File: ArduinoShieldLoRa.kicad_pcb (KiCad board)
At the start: 2 copper layers, 68.6 x 53.3 mm, 17 parts, among them J1 CONN_01X03, P1 Power, P2 Analog, P3 Digital, P4 Digital, P5 CONN_01X01, P6 CONN_01X01, P7 CONN_01X01, P8 CONN_01X01, U1 RFM95, U2 74HC4050D, U3 AP2112K-3.3

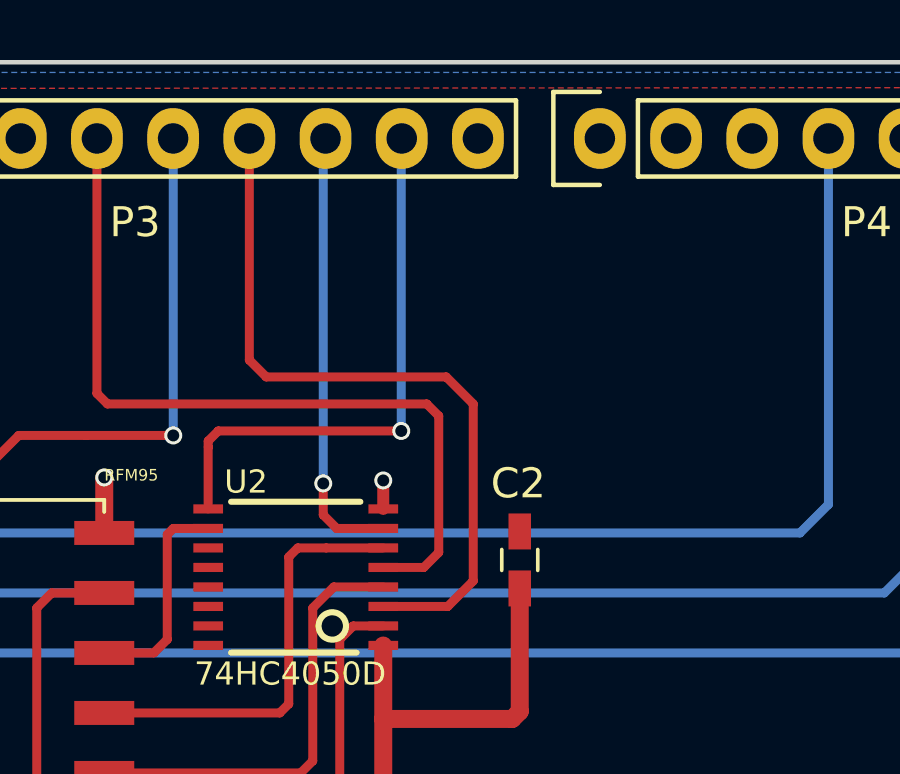
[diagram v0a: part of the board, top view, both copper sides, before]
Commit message: Add resistors
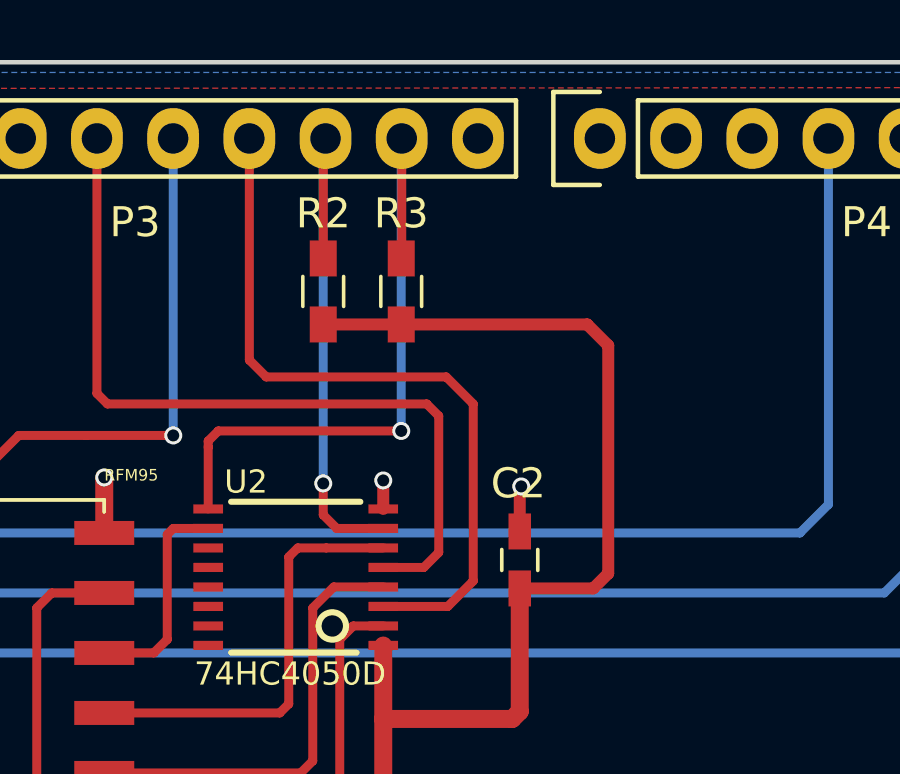
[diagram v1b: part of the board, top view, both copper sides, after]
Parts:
- added R2: 100k, Resistors_SMD:R_0603_HandSoldering, F.Cu at (147.5, 80.7)
- added R3: 100k, Resistors_SMD:R_0603_HandSoldering, F.Cu at (150.1, 80.7)
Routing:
- net +3V3: track 66.5 -> 87.1 mm
- net /10(**/SS): track 14.8 -> 18.8 mm
- net /9(**): track 18.6 -> 22.6 mm
- net GND: track 30.8 -> 32.3 mm, vias 5 -> 6
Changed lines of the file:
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@@
 (kicad_pcb (version 4) (host pcbnew 4.0.6)
   (general
-    (links 38)
-    (no_connects 11)
+    (links 42)
+    (no_connects 14)
     (area 110.922999 72.949999 179.653001 126.440001)
     (thickness 1.6)
     (drawings 27)
-    (tracks 137)
+    (tracks 150)
     (zones 0)
-    (modules 17)
+    (modules 19)
     (nets 52)
   )
@@
       (net 30 +3V3))
   )
+  (module Resistors_SMD:R_0603_HandSoldering (layer F.Cu)
+    (at 147.498 80.665 90)
+    (descr "Resistor SMD 0603, hand soldering")
+    (tags "resistor 0603")
+    (attr smd)
+    (fp_text reference R2 (at 2.6 0 180) (layer F.SilkS)
+      (effects (font (size 1 1) (thickness 0.15)))
+    )
+    (fp_text value 100k (at 0 1.55 90) (layer F.Fab)
+      (effects (font (size 1 1) (thickness 0.15)))
+    )
+    (fp_text user %R (at 0 0 90) (layer F.Fab)
+      (effects (font (size 0.5 0.5) (thickness 0.075)))
+    )
+    (fp_line (start -0.8 0.4) (end -0.8 -0.4) (layer F.Fab) (width 0.1))
+    (fp_line (start 0.8 0.4) (end -0.8 0.4) (layer F.Fab) (width 0.1))
+    (fp_line (start 0.8 -0.4) (end 0.8 0.4) (layer F.Fab) (width 0.1))
+    (fp_line (start -0.8 -0.4) (end 0.8 -0.4) (layer F.Fab) (width 0.1))
+    (fp_line (start 0.5 0.68) (end -0.5 0.68) (layer F.SilkS) (width 0.12))
+    (fp_line (start -0.5 -0.68) (end 0.5 -0.68) (layer F.SilkS) (width 0.12))
+    (fp_line (start -1.96 -0.7) (end 1.95 -0.7) (layer F.CrtYd) (width 0.05))
+    (fp_line (start -1.96 -0.7) (end -1.96 0.7) (layer F.CrtYd) (width 0.05))
+    (fp_line (start 1.95 0.7) (end 1.95 -0.7) (layer F.CrtYd) (width 0.05))
+    (fp_line (start 1.95 0.7) (end -1.96 0.7) (layer F.CrtYd) (width 0.05))
+    (pad 1 smd rect (at -1.1 0 90) (size 1.2 0.9) (layers F.Cu F.Paste F.Mask)
+      (net 30 +3V3))
+    (pad 2 smd rect (at 1.1 0 90) (size 1.2 0.9) (layers F.Cu F.Paste F.Mask)
+      (net 28 "/10(**/SS)"))
+    (model ${KISYS3DMOD}/Resistors_SMD.3dshapes/R_0603.wrl
+      (at (xyz 0 0 0))
+      (scale (xyz 1 1 1))
+      (rotate (xyz 0 0 0))
+    )
+  )
+  (module Resistors_SMD:R_0603_HandSoldering (layer F.Cu)
+    (at 150.098 80.665 90)
+    (descr "Resistor SMD 0603, hand soldering")
+    (tags "resistor 0603")
+    (attr smd)
+    (fp_text reference R3 (at 2.6 0 180) (layer F.SilkS)
+      (effects (font (size 1 1) (thickness 0.15)))
+    )
+    (fp_text value 100k (at 0 1.55 90) (layer F.Fab)
+      (effects (font (size 1 1) (thickness 0.15)))
+    )
+    (fp_text user %R (at 0 0 90) (layer F.Fab)
+      (effects (font (size 0.5 0.5) (thickness 0.075)))
+    )
+    (fp_line (start -0.8 0.4) (end -0.8 -0.4) (layer F.Fab) (width 0.1))
+    (fp_line (start 0.8 0.4) (end -0.8 0.4) (layer F.Fab) (width 0.1))
+    (fp_line (start 0.8 -0.4) (end 0.8 0.4) (layer F.Fab) (width 0.1))
+    (fp_line (start -0.8 -0.4) (end 0.8 -0.4) (layer F.Fab) (width 0.1))
+    (fp_line (start 0.5 0.68) (end -0.5 0.68) (layer F.SilkS) (width 0.12))
+    (fp_line (start -0.5 -0.68) (end 0.5 -0.68) (layer F.SilkS) (width 0.12))
+    (fp_line (start -1.96 -0.7) (end 1.95 -0.7) (layer F.CrtYd) (width 0.05))
+    (fp_line (start -1.96 -0.7) (end -1.96 0.7) (layer F.CrtYd) (width 0.05))
+    (fp_line (start 1.95 0.7) (end 1.95 -0.7) (layer F.CrtYd) (width 0.05))
+    (fp_line (start 1.95 0.7) (end -1.96 0.7) (layer F.CrtYd) (width 0.05))
+    (pad 1 smd rect (at -1.1 0 90) (size 1.2 0.9) (layers F.Cu F.Paste F.Mask)
+      (net 30 +3V3))
+    (pad 2 smd rect (at 1.1 0 90) (size 1.2 0.9) (layers F.Cu F.Paste F.Mask)
+      (net 13 "/9(**)"))
+    (model ${KISYS3DMOD}/Resistors_SMD.3dshapes/R_0603.wrl
+      (at (xyz 0 0 0))
+      (scale (xyz 1 1 1))
+      (rotate (xyz 0 0 0))
+    )
+  )
   (gr_text 1 (at 138.938 121.285 90) (layer F.SilkS)
     (effects (font (size 1 1) (thickness 0.15)))
@@
   (segment (start 149.148 112.6651) (end 149.148 115.465) (width 0.6) (layer F.Cu) (net 3))
   (segment (start 149.148 115.465) (end 149.048 115.565) (width 0.6) (layer F.Cu) (net 3))
+  (segment (start 154.048 88.665) (end 154.048 87.215) (width 0.4) (layer F.Cu) (net 4))
+  (segment (start 154.048 87.215) (end 154.098 87.165) (width 0.4) (layer F.Cu) (net 4))
+  (via (at 154.098 87.165) (size 0.6) (drill 0.4) (layers F.Cu B.Cu) (net 4))
   (segment (start 149.498 87.915) (end 149.498 86.965) (width 0.4) (layer F.Cu) (net 4))
   (via (at 149.498 86.965) (size 0.6) (drill 0.4) (layers F.Cu B.Cu) (net 4))
@@
   (segment (start 150.948 115.565) (end 150.948 114.965) (width 0.6) (layer F.Cu) (net 4))
   (segment (start 150.098 112.6651) (end 150.098 114.015) (width 0.6) (layer F.Cu) (net 4))
+  (segment (start 150.114 75.565) (end 150.114 79.549) (width 0.3) (layer F.Cu) (net 13))
+  (segment (start 150.114 79.549) (end 150.098 79.565) (width 0.3) (layer F.Cu) (net 13))
   (segment (start 150.098 85.315) (end 150.098 75.581) (width 0.3) (layer B.Cu) (net 13))
   (segment (start 150.098 75.581) (end 150.114 75.565) (width 0.3) (layer B.Cu) (net 13))
@@
   (segment (start 150.848 89.865) (end 151.348 89.365) (width 0.3) (layer F.Cu) (net 27))
   (segment (start 149.498 89.865) (end 150.848 89.865) (width 0.3) (layer F.Cu) (net 27))
+  (segment (start 147.498 79.565) (end 147.498 75.641) (width 0.3) (layer F.Cu) (net 28))
+  (segment (start 147.498 75.641) (end 147.574 75.565) (width 0.3) (layer F.Cu) (net 28))
   (segment (start 147.498 87.065) (end 147.498 75.641) (width 0.3) (layer B.Cu) (net 28))
   (segment (start 147.498 75.641) (end 147.574 75.565) (width 0.3) (layer B.Cu) (net 28))
@@
   (via (at 147.498 87.065) (size 0.6) (drill 0.4) (layers F.Cu B.Cu) (net 28))
   (segment (start 149.498 88.565) (end 147.948 88.565) (width 0.3) (layer F.Cu) (net 28))
+  (segment (start 156.998 90.065) (end 156.498 90.565) (width 0.4) (layer F.Cu) (net 30))
+  (segment (start 156.498 90.565) (end 154.048 90.565) (width 0.4) (layer F.Cu) (net 30))
+  (segment (start 156.998 82.465) (end 156.998 90.065) (width 0.4) (layer F.Cu) (net 30))
+  (segment (start 156.298 81.765) (end 156.998 82.465) (width 0.4) (layer F.Cu) (net 30))
+  (segment (start 150.098 81.765) (end 156.298 81.765) (width 0.4) (layer F.Cu) (net 30))
+  (segment (start 147.498 81.765) (end 150.098 81.765) (width 0.4) (layer F.Cu) (net 30))
   (segment (start 149.148 110.0649) (end 149.148 105.865) (width 0.6) (layer F.Cu) (net 30))
   (segment (start 149.148 105.865) (end 149.148 100.165) (width 0.6) (layer F.Cu) (net 30))
